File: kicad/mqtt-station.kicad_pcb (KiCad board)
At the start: 2 copper layers, 65 x 56 mm, 21 parts, among them J101 Conn_01x04, J102 Conn_02x07_Odd_Even, J103 Conn_01x02, J104 Conn_01x06, P1 Conn_02x20_Odd_Even, Q101 Q_NMOS_GSD, Q102 Q_PMOS_GSD, Q103 Q_PMOS_GSD, Q104 Q_PMOS_GSD, U101 ESP-WROOM-32

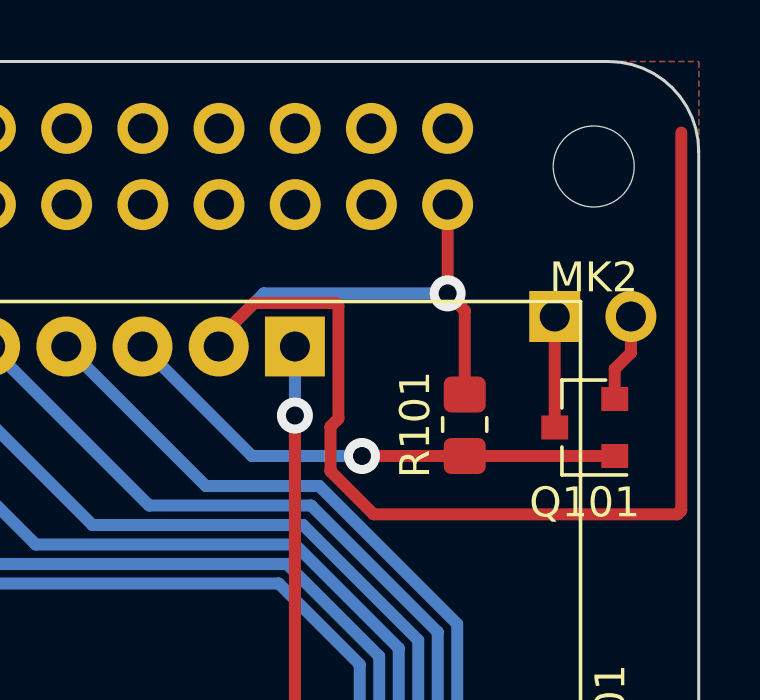
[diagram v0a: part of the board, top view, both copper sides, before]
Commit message: change dir order
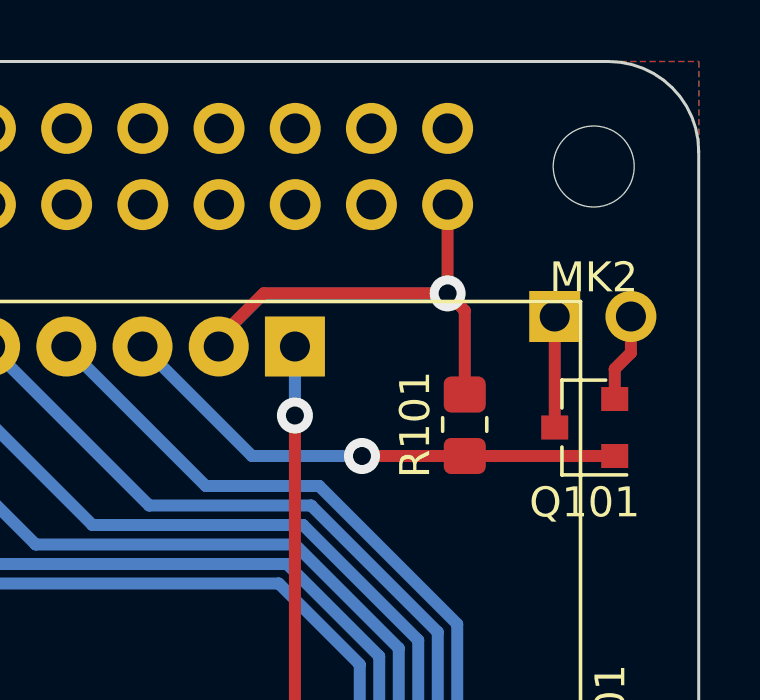
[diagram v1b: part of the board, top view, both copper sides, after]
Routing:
- net GND: track 113.2 -> 86.4 mm

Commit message: wip
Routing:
- net GND: track 86.4 -> 80.0 mm
- net /pwm_led_re: track 9.85 -> 15.5 mm, vias 1 -> 0
- net /pwm_led_bl: track 7.34 -> 11.1 mm, vias 1 -> 0
- net +3V3: track 136.6 -> 133.6 mm, vias 6 -> 3
- net /pwm_led_gr: track 6.14 -> 8.89 mm, vias 1 -> 0
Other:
- net class Default: via_dia 1.2 -> 0.6; via_drill 0.6 -> 0.3
